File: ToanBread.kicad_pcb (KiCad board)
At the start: 2 copper layers, 53.3 x 83.8 mm, 35 parts, among them J1 PJ-059A, J2 AUDIO_IN, J3 VBIAS_OUT, J4 9V_OUT, J5 AUDIO_OUT, J6 EFF_OUT, J7 EFF_IN, U1 LM4562NA

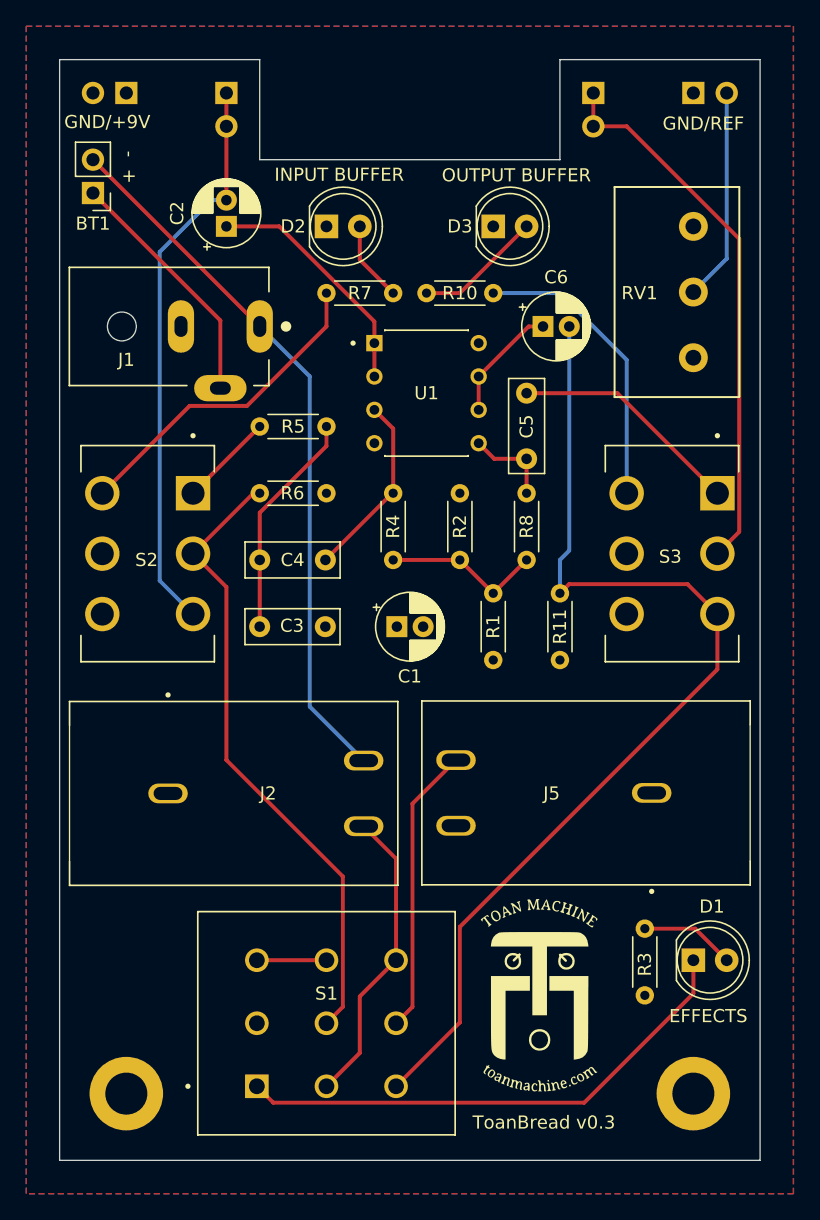
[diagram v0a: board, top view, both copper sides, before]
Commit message: Fix resistor footprints
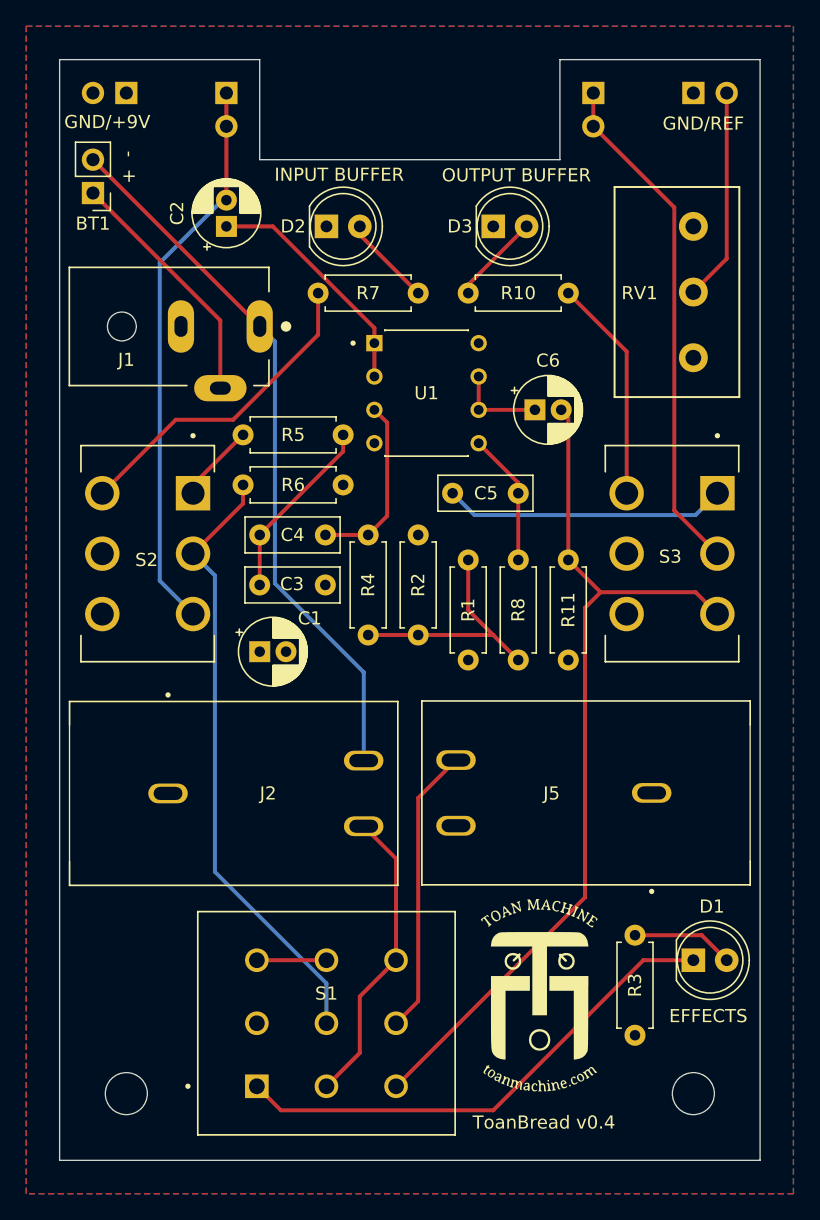
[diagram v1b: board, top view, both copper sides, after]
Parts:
- removed MHL, MHR: MountingHole_3.2mm_M3_DIN965_Pad, MountingHole:MountingHole_3.2mm_M3_DIN965_Pad
- added H1: MountingHole, MountingHole:MountingHole_3.2mm_M3_DIN965, F.Cu at (124.5, 127.0)
- added H2: MountingHole, MountingHole:MountingHole_3.2mm_M3_DIN965, F.Cu at (167.6, 127.0)
- R1, R10, R11, R2, R3, R4, R5, R6, R7, R8: footprint Resistor_THT:R_Axial_DIN0204_L3.6mm_D1.6mm_P5.08mm_Horizontal -> Resistor_THT:R_Axial_DIN0207_L6.3mm_D2.5mm_P7.62mm_Horizontal
- moved C1 10.6 mm to (134.6, 93.3)
- moved C5 9.48 mm to (149.3, 81.3), turned to 0 degrees
- moved R8 7.65 mm to (154.3, 94.0)
- moved R2 6.54 mm to (146.7, 92.1)
- moved C6 6.38 mm to (155.6, 74.9)
- moved R4 6.02 mm to (142.9, 92.1)
- moved R10 3.18 mm to (150.5, 66.0)
- moved C3 3.17 mm to (139.6, 88.3)
- moved C4 1.91 mm to (134.6, 84.5)
- moved R1 1.91 mm to (150.5, 94.0)
- moved R6 1.42 mm to (133.3, 80.6)
- moved R5 1.42 mm to (133.3, 76.8)
- moved R3 0.90 mm to (163.2, 114.9)
- moved R11 0.64 mm to (158.1, 94.0)
- moved R7 0.63 mm to (139.1, 66.0)
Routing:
- net BUF2_{OUT}: track 79.9 -> 68.8 mm
- net 4V5: track 12.3 -> 18.7 mm
- net Net-(R10-Pad2): track 22.4 -> 17.1 mm
- net Net-(C5-Pad1): track 17.7 -> 21.5 mm
- net Net-(C5-Pad2): track 6.76 -> 10.1 mm
- net Net-(C3-Pad2): track 17.3 -> 14.1 mm
- net Net-(J7-Pin_1): track 41.9 -> 39.0 mm
- net Net-(D3-A): track 9.72 -> 6.92 mm
- net Net-(C6-Pad1): track 9.02 -> 6.83 mm
- net BUF1_{IN}: track 48.0 -> 46.8 mm
- net Net-(R5-Pad1): track 7.18 -> 6.02 mm
- net Net-(D1-K): track 39.7 -> 38.7 mm
- net Net-(D2-A): track 6.13 -> 6.92 mm
- net Net-(D1-A): track 7.23 -> 7.77 mm
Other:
- board text added: "ToanBread v0.4"
- board text removed: "ToanBread v0.3"

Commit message: Make footswitch pads bigger
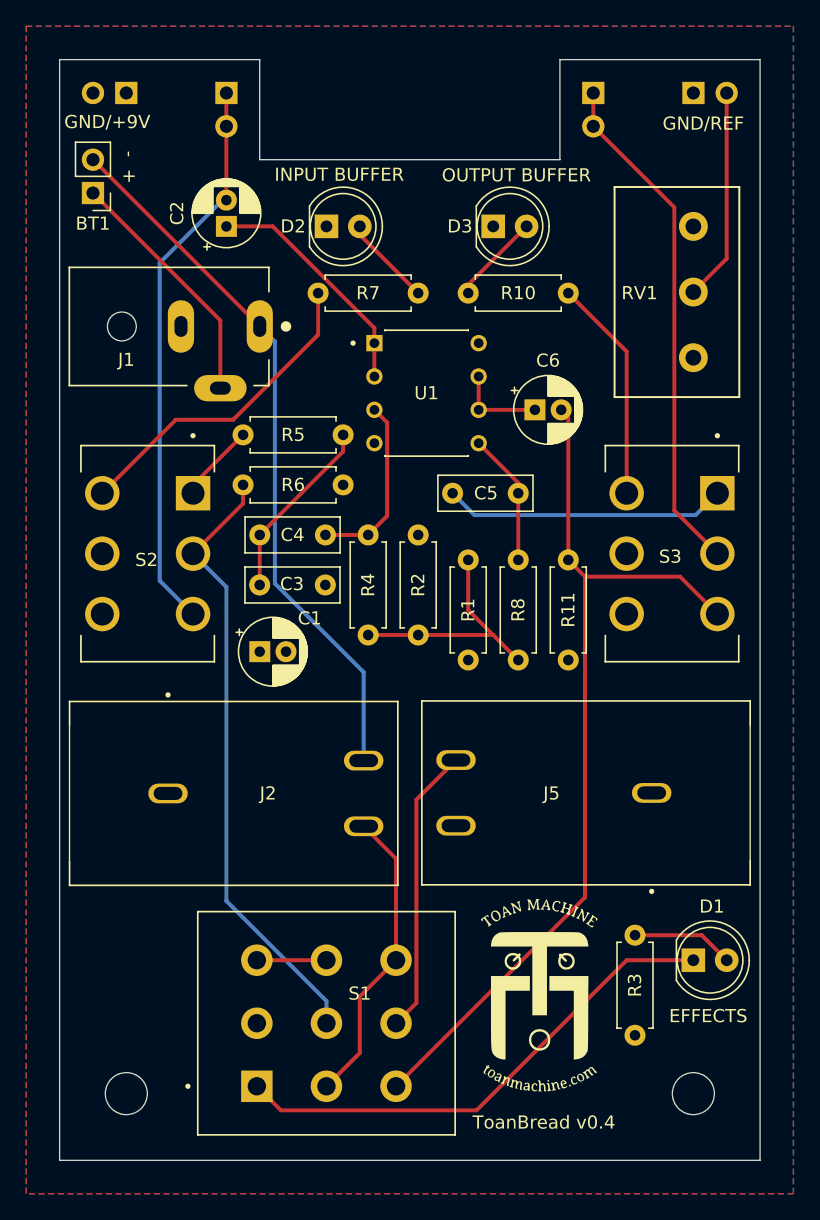
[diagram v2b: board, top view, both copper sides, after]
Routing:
- net BUF2_{OUT}: track 68.8 -> 69.5 mm
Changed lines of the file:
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@@
 		(tags "C Rect series Radial pin pitch 5.00mm  length 7mm width 2.5mm Capacitor")
 		(property "Reference" "C5"
-			(at 2.54 0 360)
+			(at 2.54 0 0)
 			(layer "F.SilkS")
 			(effects
@@
 		)
 		(property "Value" "100n"
-			(at 2.5 2.5 360)
+			(at 2.5 2.5 0)
 			(layer "F.Fab")
 			(effects
@@
 		)
 		(fp_text user "${REFERENCE}"
-			(at 2.5 0 360)
+			(at 2.5 0 0)
 			(layer "F.Fab")
 			(effects
@@
 		(at 139.7 121.64)
 		(property "Reference" "S1"
-			(at 0 -2.26 0)
+			(at 2.54 -2.26 0)
 			(layer "F.SilkS")
 			(effects
@@
 			)
 		)
-		(sheetname "Root")
-		(sheetfile "ToanBread.kicad_sch")
 		(attr through_hole)
 		(fp_line
@@
 		(pad "1" thru_hole rect
 			(at -5.3 4.8)
-			(size 1.8 1.8)
-			(drill 1.2)
+			(size 2.4 2.4)
+			(drill 1.4)
 			(layers "*.Cu" "*.Mask")
 			(remove_unused_layers no)
@@
 		(pad "2" thru_hole circle
 			(at -5.3 0)
-			(size 1.8 1.8)
-			(drill 1.2)
+			(size 2.4 2.4)
+			(drill 1.4)
 			(layers "*.Cu" "*.Mask")
 			(remove_unused_layers no)
@@
 		(pad "3" thru_hole circle
 			(at -5.3 -4.8)
-			(size 1.8 1.8)
-			(drill 1.2)
+			(size 2.4 2.4)
+			(drill 1.4)
 			(layers "*.Cu" "*.Mask")
 			(remove_unused_layers no)
@@
 		(pad "4" thru_hole circle
 			(at 0 4.8)
-			(size 1.8 1.8)
-			(drill 1.2)
+			(size 2.4 2.4)
+			(drill 1.4)
 			(layers "*.Cu" "*.Mask")
 			(remove_unused_layers no)
@@
 		(pad "5" thru_hole circle
 			(at 0 0)
-			(size 1.8 1.8)
-			(drill 1.2)
+			(size 2.4 2.4)
+			(drill 1.4)
 			(layers "*.Cu" "*.Mask")
 			(remove_unused_layers no)
@@
 		(pad "6" thru_hole circle
 			(at 0 -4.8)
-			(size 1.8 1.8)
-			(drill 1.2)
+			(size 2.4 2.4)
+			(drill 1.4)
 			(layers "*.Cu" "*.Mask")
 			(remove_unused_layers no)
@@
 		(pad "7" thru_hole circle
 			(at 5.3 4.8)
-			(size 1.8 1.8)
-			(drill 1.2)
+			(size 2.4 2.4)
+			(drill 1.4)
 			(layers "*.Cu" "*.Mask")
 			(remove_unused_layers no)
@@
 		(pad "8" thru_hole circle
 			(at 5.3 0)
-			(size 1.8 1.8)
-			(drill 1.2)
+			(size 2.4 2.4)
+			(drill 1.4)
 			(layers "*.Cu" "*.Mask")
 			(remove_unused_layers no)
@@
 		(pad "9" thru_hole circle
 			(at 5.3 -4.8)
-			(size 1.8 1.8)
-			(drill 1.2)
+			(size 2.4 2.4)
+			(drill 1.4)
 			(layers "*.Cu" "*.Mask")
 			(remove_unused_layers no)
@@
 	)
 	(segment
-		(start 145 126.44)
-		(end 159.385 112.055)
+		(start 159.385 87.63)
+		(end 158.115 86.36)
 		(width 0.3)
 		(layer "F.Cu")
@@
 	(segment
 		(start 159.385 112.055)
-		(end 159.385 90.005)
-		(width 0.3)
-		(layer "F.Cu")
-		(net 12)
-	)
-	(segment
-		(start 169.47 90.48)
-		(end 167.8075 88.8175)
+		(end 159.385 87.63)
 		(width 0.3)
 		(layer "F.Cu")
@@
 	)
 	(segment
-		(start 160.5725 88.8175)
-		(end 158.115 86.36)
+		(start 166.62 87.63)
+		(end 159.385 87.63)
 		(width 0.3)
 		(layer "F.Cu")
@@
 	)
 	(segment
-		(start 159.385 90.005)
-		(end 160.5725 88.8175)
+		(start 158.115 86.36)
+		(end 158.115 75.47)
 		(width 0.3)
 		(layer "F.Cu")
@@
 	)
 	(segment
-		(start 158.115 86.36)
-		(end 158.115 75.47)
+		(start 169.47 90.48)
+		(end 166.62 87.63)
 		(width 0.3)
 		(layer "F.Cu")
@@
 	)
 	(segment
-		(start 167.8075 88.8175)
-		(end 160.5725 88.8175)
+		(start 145 126.44)
+		(end 159.385 112.055)
 		(width 0.3)
 		(layer "F.Cu")
@@
 	)
 	(segment
-		(start 152.4 128.27)
-		(end 163.83 116.84)
+		(start 134.4 126.44)
+		(end 136.23 128.27)
 		(width 0.3)
 		(layer "F.Cu")
@@
 	)
 	(segment
-		(start 134.4 126.44)
-		(end 136.23 128.27)
+		(start 151.13 128.27)
+		(end 162.56 116.84)
 		(width 0.3)
 		(layer "F.Cu")
@@
 	)
 	(segment
-		(start 163.83 116.84)
+		(start 162.56 116.84)
 		(end 167.64 116.84)
 		(width 0.3)
@@
 	(segment
 		(start 136.23 128.27)
-		(end 152.4 128.27)
+		(end 151.13 128.27)
 		(width 0.3)
 		(layer "F.Cu")
@@
 	)
 	(segment
+		(start 145 109.105)
+		(end 142.535 106.64)
+		(width 0.3)
+		(layer "F.Cu")
+		(net 17)
+	)
+	(segment
 		(start 145 116.84)
 		(end 145 109.105)
@@
 	)
 	(segment
-		(start 145 109.105)
-		(end 142.535 106.64)
-		(width 0.3)
-		(layer "F.Cu")
-		(net 17)
-	)
-	(segment
 		(start 170.18 63.42)
 		(end 170.18 50.8)
@@
 	)
 	(segment
-		(start 149.565 101.6)
-		(end 146.685 104.48)
+		(start 146.55 120.09)
+		(end 145 121.64)
 		(width 0.3)
 		(layer "F.Cu")
@@
 	)
 	(segment
-		(start 146.685 104.48)
-		(end 146.685 119.955)
+		(start 149.565 101.6)
+		(end 146.55 104.615)
 		(width 0.3)
 		(layer "F.Cu")
@@
 	)
 	(segment
-		(start 146.685 119.955)
-		(end 145 121.64)
+		(start 146.55 104.615)
+		(end 146.55 120.09)
 		(width 0.3)
 		(layer "F.Cu")
@@
 	)
 	(segment
-		(start 139.7 118.607767)
-		(end 131.2025 110.110267)
+		(start 132.08 112.327968)
+		(end 132.08 88.42)
 		(width 0.3)
 		(layer "B.Cu")
@@
 	)
 	(segment
-		(start 131.2025 110.110267)
-		(end 131.2025 87.5425)
+		(start 132.08 88.42)
+		(end 129.54 85.88)
 		(width 0.3)
 		(layer "B.Cu")
@@
 	)
 	(segment
-		(start 131.2025 87.5425)
-		(end 129.54 85.88)
+		(start 139.7 121.64)
+		(end 139.7 119.947968)
 		(width 0.3)
 		(layer "B.Cu")
@@
 	)
 	(segment
-		(start 139.7 121.64)
-		(end 139.7 118.607767)
+		(start 139.7 119.947968)
+		(end 132.08 112.327968)
 		(width 0.3)
 		(layer "B.Cu")

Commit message: Fix input and output buffer switches
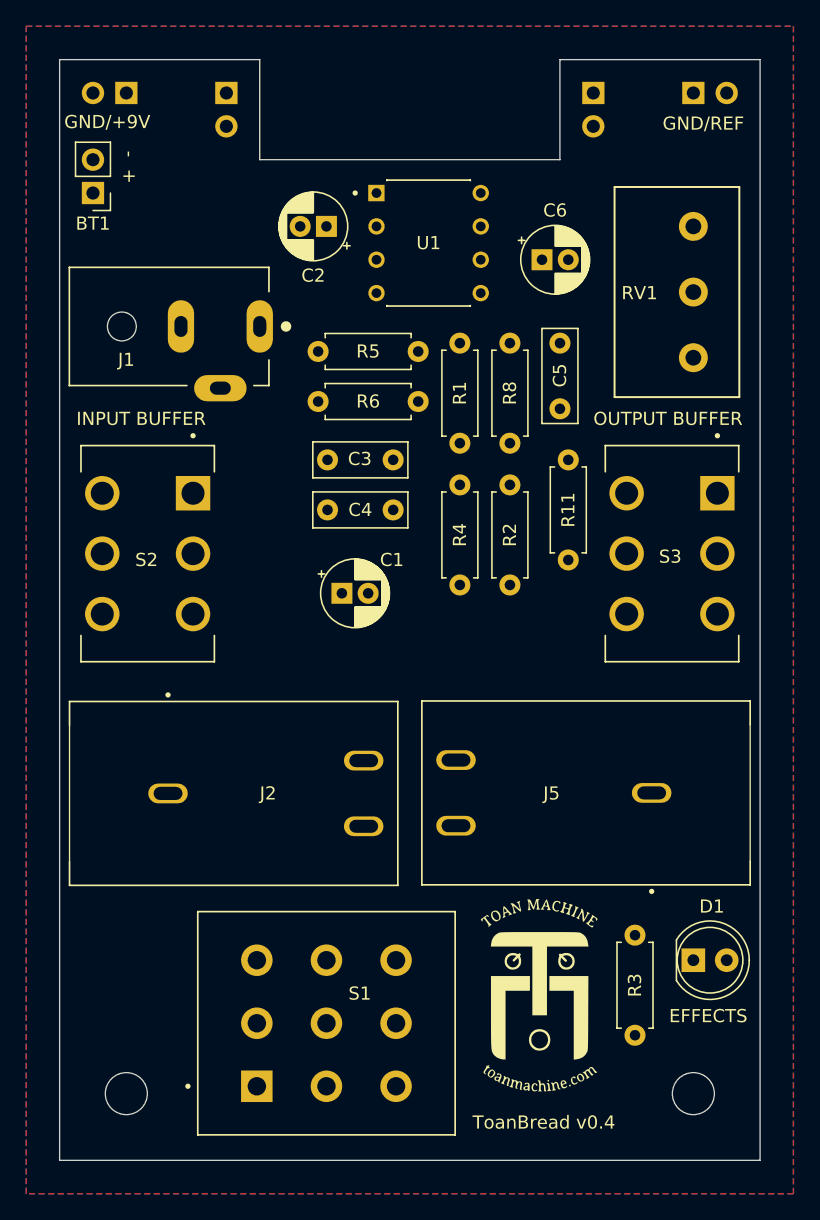
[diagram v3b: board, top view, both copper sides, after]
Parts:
- removed D2: INPUT_BUF, LED_THT:LED_D5.0mm
- removed D3: OUTPUT_BUF, LED_THT:LED_D5.0mm
- removed R10, R7: 4.7k, Resistor_THT:R_Axial_DIN0207_L6.3mm_D2.5mm_P7.62mm_Horizontal
- moved R1 16.5 mm to (149.9, 77.5)
- moved R8 16.5 mm to (153.7, 77.5)
- moved R4 13.4 mm to (149.9, 80.6), turned to -90 degrees
- moved R2 13.4 mm to (153.7, 80.6), turned to -90 degrees
- moved C6 11.4 mm to (156.1, 63.5)
- moved U1 11.4 mm to (147.5, 62.2)
- moved C3 10.8 mm to (144.8, 78.7)
- moved C5 10.4 mm to (157.5, 74.8), turned to 90 degrees
- moved R5 8.54 mm to (139.1, 70.5)
- moved R6 8.54 mm to (139.1, 74.3)
- moved C1 7.67 mm to (140.9, 88.9)
- moved R11 7.62 mm to (158.1, 86.4)
- moved C2 7.62 mm to (139.7, 61.0), turned to 180 degrees
- moved C4 5.50 mm to (139.8, 82.5)
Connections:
- C2 pad 2: Net-(J6-Pin_1) -> Net-(C2-Pad2)
- C6 pad 2: BUF2_{OUT} -> Net-(C6-Pad2)
- S2 pad 3: Net-(J6-Pin_1) -> Net-(S2-Pad3)
- S2 pad 4: Net-(R7-Pad1) -> Net-(C2-Pad2)
- S2 pad 5: +9V -> Net-(J6-Pin_1)
- S2 pad 6: unconnected-(S2-Pad6) -> Net-(S2-Pad3)
- S3 pad 3: BUF2_{OUT} -> Net-(S3-Pad3)
- S3 pad 4: Net-(R10-Pad2) -> Net-(C6-Pad2)
- S3 pad 5: +9V -> BUF2_{OUT}
- S3 pad 6: unconnected-(S3-Pad6) -> Net-(S3-Pad3)
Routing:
- net BUF2_{OUT}: track 69.5 -> 0.00 mm
- net Net-(BT1--): track 54.3 -> 0.00 mm
- net BUF1_{IN}: track 46.8 -> 0.00 mm
- net Net-(J6-Pin_1): track 43.0 -> 0.00 mm
- net Net-(J7-Pin_1): track 39.0 -> 0.00 mm
- net Net-(D1-K): track 38.7 -> 0.00 mm
- net Net-(R7-Pad1): track 24.6 -> 0.00 mm
- net SIG: track 23.0 -> 0.00 mm
- net Net-(J5-Pad2): track 21.9 -> 0.00 mm
- net Net-(C5-Pad1): track 21.5 -> 0.00 mm
- net Net-(BT1-+): track 18.9 -> 0.00 mm
- net 4V5: track 18.7 -> 0.00 mm
- net Net-(C2-Pad1): track 18.2 -> 0.00 mm
- net Net-(R10-Pad2): track 17.1 -> 0.00 mm
- net Net-(J3-Pin_2): track 16.2 -> 0.00 mm
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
